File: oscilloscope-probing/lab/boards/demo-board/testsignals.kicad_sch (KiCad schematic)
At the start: 40 parts, among them J10 SMA-J-P-H-ST-EM1, J11 TESTCLIP, J12 TESTCLIP, J13 TESTCLIP, J15 TESTCLIP, J16 SMA-J-P-H-ST-EM1, J17 SMA-J-P-H-ST-EM1, J18 SMA-J-P-H-ST-EM1, J19 SMA-J-P-H-ST-EM1, J20 SMA-J-P-H-ST-EM1, J21 SMA-J-P-H-ST-EM1, J7 SMA-J-P-H-ST-EM1, J8 SMA-J-P-H-ST-EM1, J9 SMA-J-P-H-ST-EM1, U10 19-C47/RSGHBHC-5V01/2T, U11 19-C47/RSGHBHC-5V01/2T, U12 19-C47/RSGHBHC-5V01/2T, U13 19-C47/RSGHBHC-5V01/2T, U26 74LVC1T45, U4 XC7A35T-2FGG484I, U9 SIT9121AI-2BF-XXS156.250000G

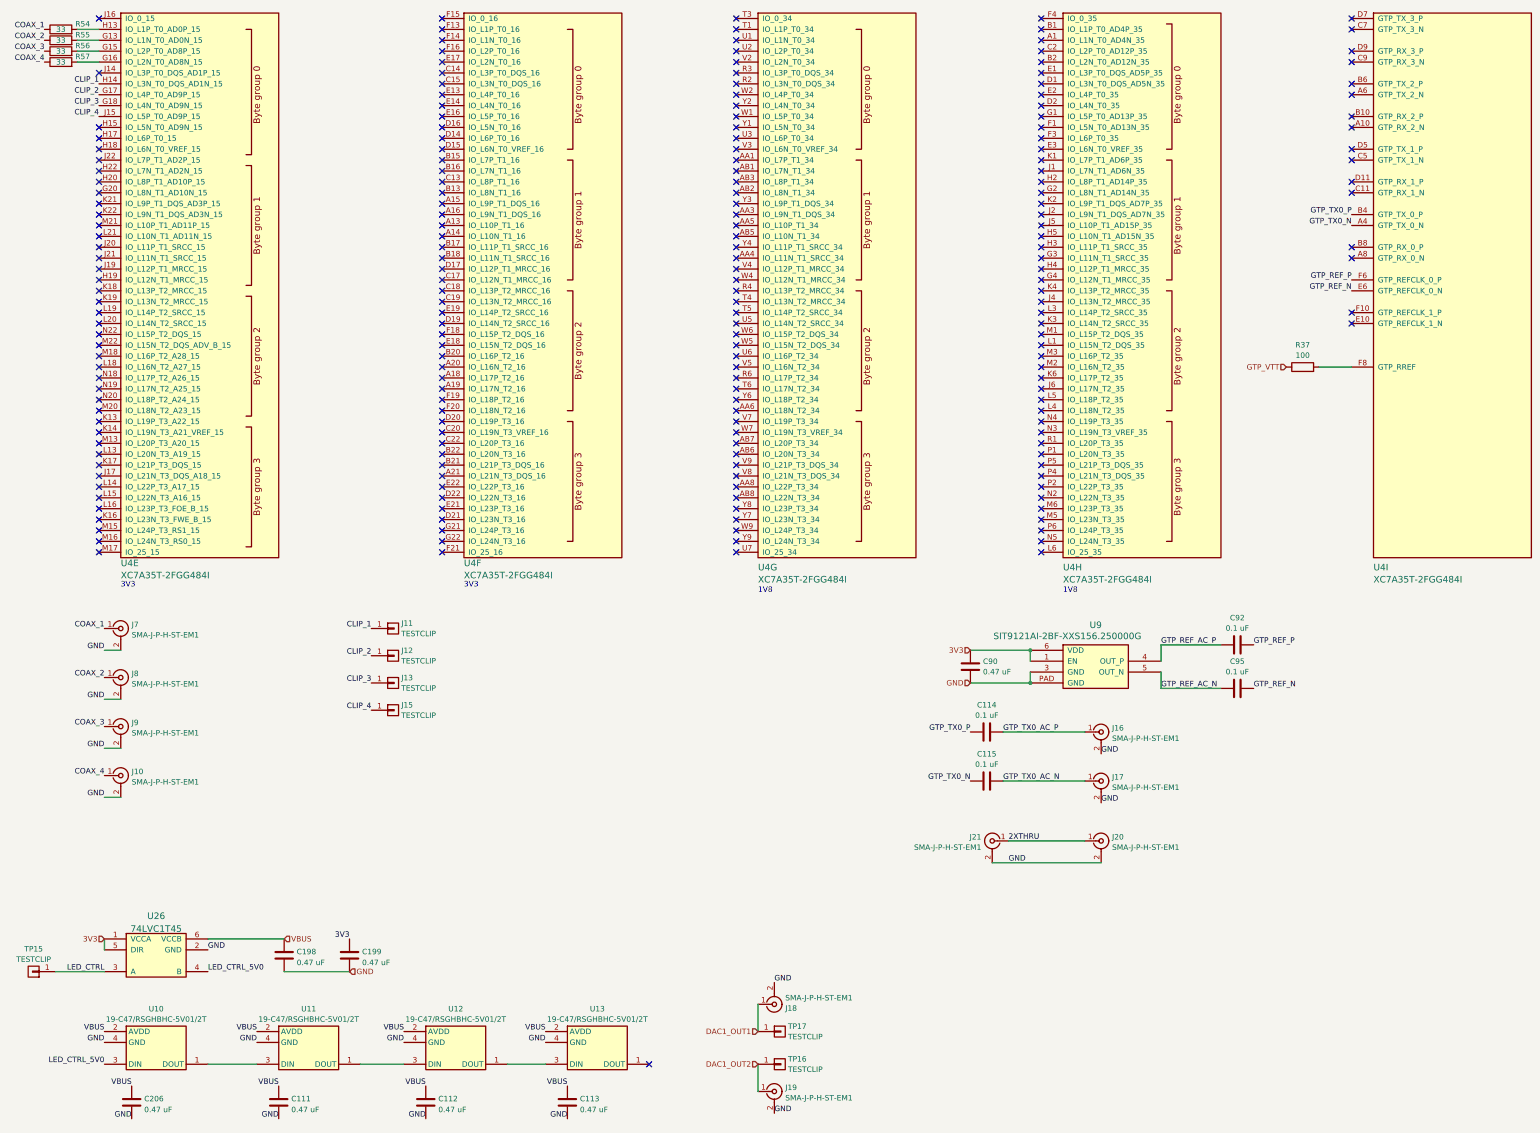
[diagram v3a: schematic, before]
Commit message: Continued demo board layout
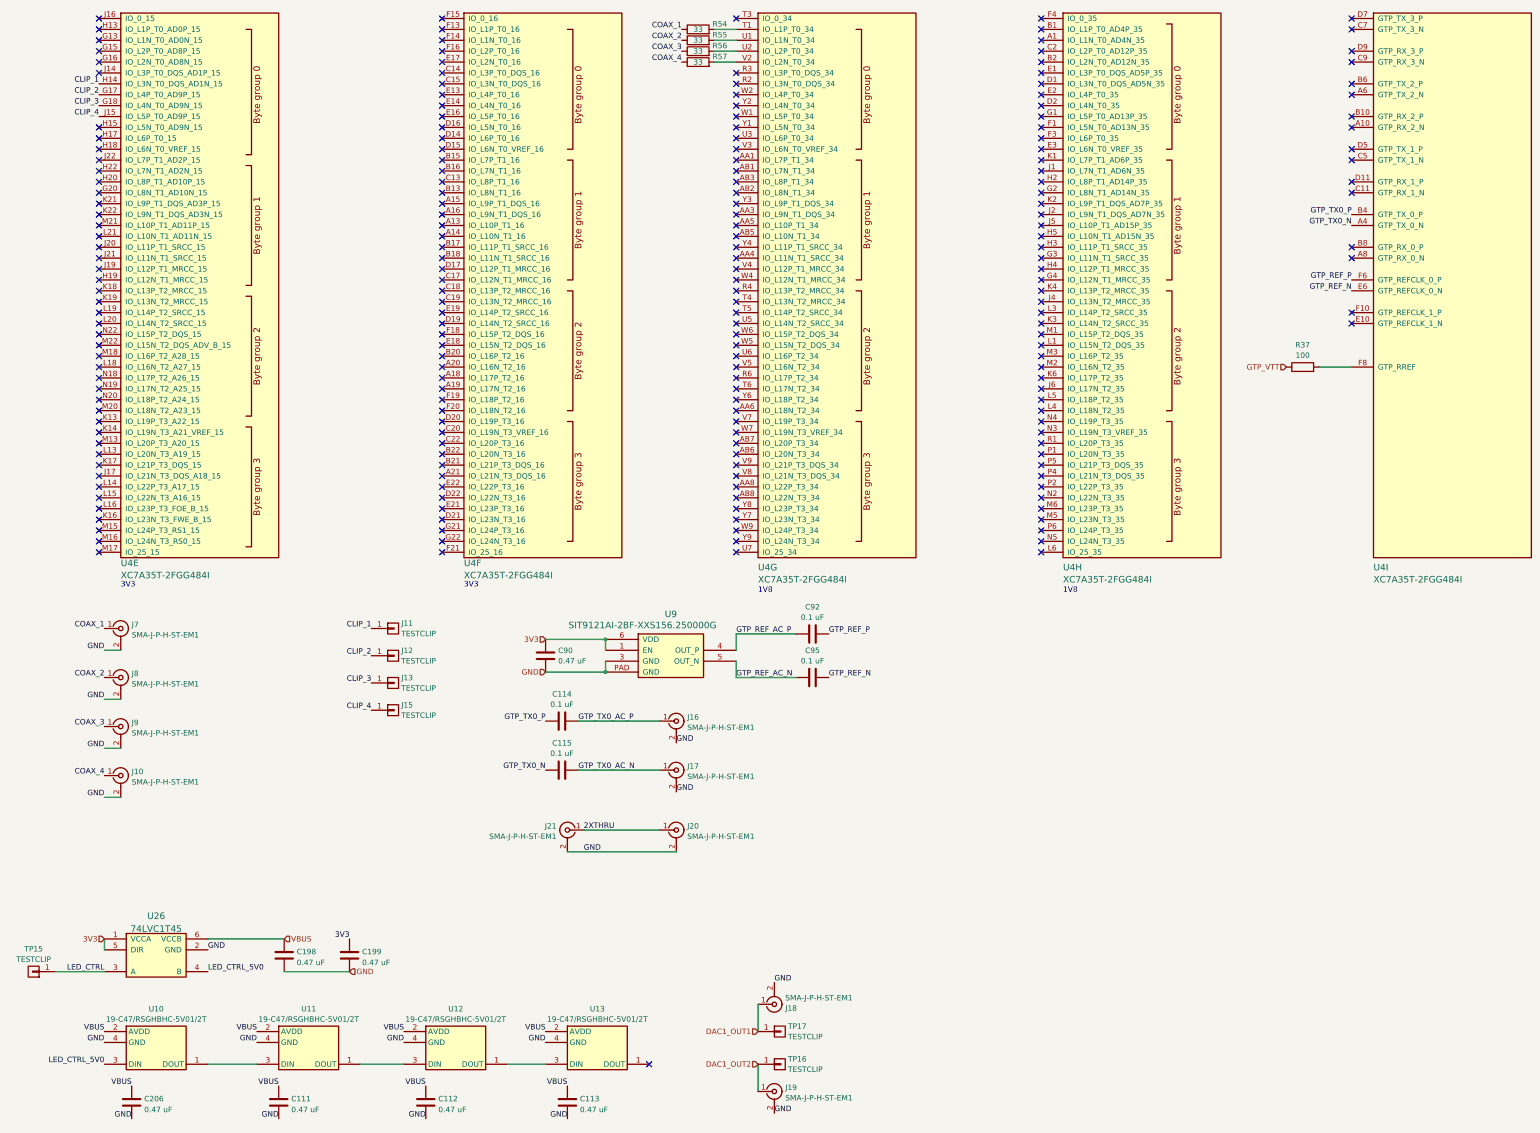
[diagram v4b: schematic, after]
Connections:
- net at R54.2: now also U4.T1 (IO_L1P_T0_34); no longer U4.H13 (IO_L1P_T0_AD0P_15)
- net at R56.2: now also U4.U2 (IO_L2P_T0_34); no longer U4.G15 (IO_L2P_T0_AD8P_15)
- net at U4.G13 (IO_L1N_T0_AD0N_15): no longer R55.2
- net at U4.G16 (IO_L2N_T0_AD8N_15): no longer R57.2
- net at U4.U1 (IO_L1N_T0_34): now also R55.2
- net at U4.V2 (IO_L2N_T0_34): now also R57.2
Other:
- moved on the sheet: C114, C115, C90, C92, C95, J16, J17, J20, J21, R54, R55, R56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

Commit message: Continued demo board layout
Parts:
- added D10, D11, D8, D9: GREEN, azonenberg_pcb:EIA_0402_LED, symbol device:LED
- added R63, R64, R65, R66: 33K, azonenberg_pcb:EIA_0402_RES_NOSILK, symbol device:R
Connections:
- net GND: now also D10.1 (K), D11.1 (K), D8.1 (K), D9.1 (K)
- net FPGA_LED0: now reaches U4.B22 (IO_L20N_T3_16)
- net FPGA_LED0: now also R63.1
- net FPGA_LED1: now reaches U4.C22 (IO_L20P_T3_16)
- net FPGA_LED1: now also R64.1
- net FPGA_LED2: now reaches U4.D22 (IO_L22N_T3_16)
- net FPGA_LED2: now also R65.1
- net FPGA_LED3: now reaches U4.E22 (IO_L22P_T3_16)
- net FPGA_LED3: now also R66.1
- new net: D8.2 (A), R63.2
- new net: D11.2 (A), R66.2
- new net: D9.2 (A), R64.2
- new net: D10.2 (A), R65.2
- no-connect marks 209 -> 205

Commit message: Continued demo board layout
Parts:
- added C124, C125: 0.1 uF, azonenberg_pcb:EIA_0402_CAP_NOSILK, symbol device:C
- added J22, J23: SMA-J-P-H-ST-EM1, azonenberg_pcb:CONN_SMA_EDGE_SAMTEC_SMA_J_P_H_ST_EM1, symbol conn:CONN_COAXIAL
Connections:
- net 2XTHRU: now also J22.1 (In), J23.1 (In); no longer J20.1 (In), J21.1 (In)
- net GND: now also J22.2 (Ext), J23.2 (Ext)
- net GTP_TX1_N: now reaches U4.C5 (GTP_TX_1_N)
- net GTP_TX1_N: now also C125.1
- net GTP_TX1_P: now reaches U4.D5 (GTP_TX_1_P)
- net GTP_TX1_P: now also C124.1
- new net GTP_TX1_AC_N: C125.2, J21.1 (In)
- new net GTP_TX1_AC_P: C124.2, J20.1 (In)
- no-connect marks 205 -> 203
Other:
- company: (none) -> Antikernel Labs
- title: (none) -> Oscilloscope Demo Board
- moved on the sheet: J21

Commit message: Continued routing demo board
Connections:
- net LED_CTRL: now also U4.F21 (IO_25_16)
- no-connect marks 203 -> 202
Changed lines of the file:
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@@
-	)
-	(no_connect
-		(at 123.19 144.78)
 	)
 	(no_connect
@@
 		(effects
 			(font
+				(size 1.27 1.27)
+			)
+			(justify right bottom)
+		)
+	)
+	(label "LED_CTRL"
+		(at 123.19 144.78 180)
+		(effects
+			(font

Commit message: Continued demo board layout
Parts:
- added J6: CONN_01X06, azonenberg_pcb:CONN_HEADER_2.54MM_1x6_REFLOW, symbol conn:CONN_01X06
- J18, J19, J22, J23: footprint azonenberg_pcb:CONN_SMA_EDGE_SAMTEC_SMA_J_P_H_ST_EM1 -> azonenberg_pcb:CONN_SMA_EDGE_SAMTEC_SMA_J_P_H_ST_EM1_NOPASTE
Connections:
- net GND: now also J6.1 (P1)
- net GTP_REF_N: now also C92.2; no longer C95.2
- net GTP_REF_P: now also C95.2; no longer C92.2
- net FPGA_UART_CTS_N: now reaches U4.A18 (IO_L17P_T2_16)
- net FPGA_UART_CTS_N: now also J6.2 (P2)
- net FPGA_UART_TX: now reaches U4.A19 (IO_L17N_T2_16)
- net FPGA_UART_TX: now also J6.4 (P4)
- net FPGA_UART_RTS_N: now reaches U4.A20 (IO_L16N_T2_16)
- net FPGA_UART_RTS_N: now also J6.6 (P6)
- net FPGA_UART_RX: now reaches U4.A21 (IO_L21N_T3_DQS_16)
- net FPGA_UART_RX: now also J6.5 (P5)
- no-connect marks 202 -> 199
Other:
- note added: "FTDI cable pinout"
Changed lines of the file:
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@@
 	(title_block
 		(title "Oscilloscope Demo Board")
-		(date "2026-08-08")
+		(date "2026-08-11")
 		(rev "0.1")
 		(company "Antikernel Labs")
@@
 		)
 	)
+	(text "FTDI cable pinout"
+		(exclude_from_sim no)
+		(at 330.2 175.26 0)
+		(effects
+			(font
+				(size 1.27 1.27)
+			)
+			(justify left)
+		)
+	)
 	(text "1V8"
 		(exclude_from_sim no)
@@
 	)
 	(no_connect
-		(at 123.19 101.6)
-	)
-	(no_connect
 		(at 123.19 63.5)
 	)
@@
 	)
 	(no_connect
-		(at 123.19 127)
-	)
-	(no_connect
 		(at 335.28 60.96)
 	)
@@
 	)
 	(no_connect
-		(at 123.19 104.14)
-	)
-	(no_connect
 		(at 123.19 91.44)
 	)
@@
 	)
 	(no_connect
-		(at 123.19 106.68)
-	)
-	(no_connect
 		(at 123.19 20.32)
 	)
@@
 		(at 123.19 114.3)
 	)
+	(no_connect
+		(at 340.36 165.1)
+	)
 	(wire
 		(pts
@@
 	)
 	(label "GTP_REF_P"
-		(at 213.36 163.83 0)
+		(at 213.36 173.99 0)
 		(effects
 			(font
@@
 		)
 	)
+	(label "GND"
+		(at 340.36 160.02 180)
+		(effects
+			(font
+				(size 1.27 1.27)
+			)
+			(justify right bottom)
+		)
+	)
 	(label "GTP_TX1_P"
 		(at 335.28 50.8 180)
@@
 		)
 	)
+	(label "FPGA_UART_CTS_N"
+		(at 340.36 162.56 180)
+		(effects
+			(font
+				(size 1.27 1.27)
+			)
+			(justify right bottom)
+		)
+	)
+	(label "FPGA_UART_TX"
+		(at 340.36 167.64 180)
+		(effects
+			(font
+				(size 1.27 1.27)
+			)
+			(justify right bottom)
+		)
+	)
 	(label "GTP_TX0_P"
 		(at 335.28 66.04 180)
@@
 		)
 	)
+	(label "FPGA_UART_CTS_N"
+		(at 123.19 104.14 180)
+		(effects
+			(font
+				(size 1.27 1.27)
+			)
+			(justify right bottom)
+		)
+	)
 	(label "VBUS"
 		(at 119.38 269.24 180)
@@
 		)
 	)
+	(label "FPGA_UART_CTS_N"
+		(at 264.16 167.64 180)
+		(effects
+			(font
+				(size 1.27 1.27)
+			)
+			(justify right bottom)
+		)
+	)
 	(label "GTP_TX1_N"
 		(at 335.28 53.34 180)
@@
 		)
 	)
+	(label "FPGA_UART_RX"
+		(at 264.16 175.26 180)
+		(effects
+			(font
+				(size 1.27 1.27)
+			)
+			(justify right bottom)
+		)
+	)
+	(label "FPGA_UART_RTS_N"
+		(at 123.19 101.6 180)
+		(effects
+			(font
+				(size 1.27 1.27)
+			)
+			(justify right bottom)
+		)
+	)
 	(label "COAX_1"
 		(at 44.45 162.56 180)
@@
 		)
 	)
+	(label "FPGA_UART_TX"
+		(at 264.16 172.72 180)
+		(effects
+			(font
+				(size 1.27 1.27)
+			)
+			(justify right bottom)
+		)
+	)
 	(label "GTP_TX0_P"
 		(at 147.32 184.15 180)
@@
 		)
 	)
+	(label "FPGA_UART_RTS_N"
+		(at 264.16 177.8 180)
+		(effects
+			(font
+				(size 1.27 1.27)
+			)
+			(justify right bottom)
+		)
+	)
 	(label "VBUS"
 		(at 80.01 256.54 180)
@@
 	)
 	(label "GTP_REF_N"
-		(at 213.36 173.99 0)
+		(at 213.36 163.83 0)
 		(effects
 			(font
@@
 		)
 	)
+	(label "FPGA_UART_RTS_N"
+		(at 340.36 172.72 180)
+		(effects
+			(font
+				(size 1.27 1.27)
+			)
+			(justify right bottom)
+		)
+	)
 	(label "VBUS"
 		(at 114.3 256.54 180)
@@
 		)
 	)
+	(label "FPGA_UART_RX"
+		(at 123.19 127 180)
+		(effects
+			(font
+				(size 1.27 1.27)
+			)
+			(justify right bottom)
+		)
+	)
 	(label "GND"
 		(at 236.22 227.33 0)
@@
 		)
 	)
+	(label "FPGA_UART_RX"
+		(at 340.36 170.18 180)
+		(effects
+			(font
+				(size 1.27 1.27)
+			)
+			(justify right bottom)
+		)
+	)
 	(label "GND"
 		(at 119.38 276.86 180)
@@
 		)
 	)
+	(label "FPGA_UART_TX"
+		(at 123.19 106.68 180)
+		(effects
+			(font
+				(size 1.27 1.27)
+			)
+			(justify right bottom)
+		)
+	)
 	(label "CLIP_1"
 		(at 43.18 35.56 180)
@@
 			)
 		)
-		(property "Footprint" "azonenberg_pcb:CONN_SMA_EDGE_SAMTEC_SMA_J_P_H_ST_EM1"
+		(property "Footprint" "azonenberg_pcb:CONN_SMA_EDGE_SAMTEC_SMA_J_P_H_ST_EM1_NOPASTE"
 			(at 200.66 270.51 0)
 			(effects
@@
 			)
 		)
-		(property "Footprint" "azonenberg_pcb:CONN_SMA_EDGE_SAMTEC_SMA_J_P_H_ST_EM1"
+		(property "Footprint" "azonenberg_pcb:CONN_SMA_EDGE_SAMTEC_SMA_J_P_H_ST_EM1_NOPASTE"
 			(at 200.66 250.19 0)
 			(effects
@@
 			)
 		)
-		(property "Footprint" "azonenberg_pcb:CONN_SMA_EDGE_SAMTEC_SMA_J_P_H_ST_EM1"
+		(property "Footprint" "azonenberg_pcb:CONN_SMA_EDGE_SAMTEC_SMA_J_P_H_ST_EM1_NOPASTE"
 			(at 236.22 210.82 0)
 			(effects
@@
 	)
 	(symbol
+		(lib_id "conn:CONN_01X06")
+		(at 345.44 166.37 0)
+		(unit 1)
+		(exclude_from_sim no)
+		(in_bom yes)
+		(on_board yes)
+		(dnp no)
+		(fields_autoplaced yes)
+		(property "Reference" "J6"
+			(at 347.345 165.1578 0)
+			(effects
+				(font
+					(size 1.27 1.27)
+				)
+				(justify left)
+			)
+		)
+		(property "Value" "CONN_01X06"
+			(at 347.345 167.5821 0)
+			(effects
+				(font
+					(size 1.27 1.27)
+				)
+				(justify left)
+			)
+		)
+		(property "Footprint" "azonenberg_pcb:CONN_HEADER_2.54MM_1x6_REFLOW"
+			(at 345.44 166.37 0)
+			(effects
+				(font
+					(size 1.27 1.27)
+				)
+				(hide yes)
+			)
+		)
+		(property "Datasheet" ""
+			(at 345.44 166.37 0)
+			(effects
+				(font
+					(size 1.27 1.27)
+				)
+				(hide yes)
+			)
+		)
+		(property "Description" "Connector, single row, 01x06, pin header"
+			(at 345.44 166.37 0)
+			(effects
+				(font
+					(size 1.27 1.27)
+				)
+				(hide yes)
+			)
+		)
+		(pin "6"
+		)
+		(pin "1"
+		)
+		(pin "5"
+		)
+		(pin "3"
+		)
+		(pin "2"
+		)
+		(pin "4"
+		)
+		(instances
+			(project "demo-board"
+				(path "/aa2d82c6-7ba7-4266-9b47-ed3339e6c556/a5c6d6a0-0eb9-4128-8a96-febfa5d4e510"
+					(reference "J6")
+					(unit 1)
+				)
+			)
+		)
+	)
+	(symbol
 		(lib_id "special-azonenberg:19-C47_RSGHBHC-5V01_2T")
 		(at 119.38 265.43 0)
@@
 			)
 		)
-		(property "Footprint" "azonenberg_pcb:CONN_SMA_EDGE_SAMTEC_SMA_J_P_H_ST_EM1"
+		(property "Footprint" "azonenberg_pcb:CONN_SMA_EDGE_SAMTEC_SMA_J_P_H_ST_EM1_NOPASTE"
 			(at 236.22 222.25 0)
 			(effects
